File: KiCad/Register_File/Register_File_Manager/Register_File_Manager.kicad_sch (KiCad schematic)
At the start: 39 parts, among them J1 Conn_01x04_Socket, J10 Conn_01x02_Socket, J11 Conn_01x02_Socket, J12 Conn_01x02_Socket, J13 Conn_01x02_Socket, J14 Conn_01x02_Socket, J15 Conn_01x02_Socket, J16 Conn_01x02_Socket, J17 Conn_01x02_Socket, J18 Conn_01x02_Socket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

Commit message: finished registier file boards
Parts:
- removed D0, D5, D6, D7: LED, LED_THT:LED_Rectangular_W3.0mm_H2.0mm, symbol Device:LED
- removed RN1: R_Network08_US, Resistor_THT:R_Array_SIP9, symbol Device:R_Network08_US
- added J21, J22, J23, J24: Conn_01x08_Socket, Connector_PinHeader_2.54mm:PinHeader_1x08_P2.54mm_Vertical, symbol Connector:Conn_01x08_Socket
- added R1, R2, R3, R4: 1k, Resistor_SMD:R_1206_3216Metric_Pad1.30x1.75mm_HandSolder, symbol Device:R_US
- added SW1: SW_SPDT, Button_Switch_THT:SW_Slide_SPDT_Angled_CK_OS102011MA1Q, symbol Switch:SW_SPDT
- added U7: 74LS245, Package_DIP:DIP-20_W7.62mm_Socket_LongPads, symbol 74xx:74LS245
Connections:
- net GND: now also D1.1 (K), D2.1 (K), D3.1 (K), D4.1 (K), SW1.1 (A), U7.10 (GND)
- net IN_EN_REG_0: now also J23.8 (Pin_8)
- net IN_EN_REG_1: now also J23.7 (Pin_7)
- net IN_EN_REG_10: now also J24.6 (Pin_6)
- net IN_EN_REG_11: now also J24.5 (Pin_5)
- net IN_EN_REG_12: now also J24.4 (Pin_4)
- net IN_EN_REG_13: now also J24.3 (Pin_3)
- net IN_EN_REG_14: now also J24.2 (Pin_2)
- net IN_EN_REG_15: now also J24.1 (Pin_1)
- net IN_EN_REG_2: now also J23.6 (Pin_6)
- net IN_EN_REG_3: now also J23.5 (Pin_5)
- net IN_EN_REG_4: now also J23.4 (Pin_4)
- net IN_EN_REG_5: now also J23.3 (Pin_3)
- net IN_EN_REG_6: now also J23.2 (Pin_2)
- net IN_EN_REG_7: now also J23.1 (Pin_1)
- net IN_EN_REG_8: now also J24.8 (Pin_8)
- net IN_EN_REG_9: now also J24.7 (Pin_7)
- net OUT_EN_REG_0: now also J21.8 (Pin_8)
- net OUT_EN_REG_1: now also J21.7 (Pin_7)
- net OUT_EN_REG_10: now also J22.6 (Pin_6)
- net OUT_EN_REG_11: now also J22.5 (Pin_5)
- net OUT_EN_REG_12: now also J22.4 (Pin_4)
- net OUT_EN_REG_13: now also J22.3 (Pin_3)
- net OUT_EN_REG_14: now also J22.2 (Pin_2)
- net OUT_EN_REG_15: now also J22.1 (Pin_1)
- net OUT_EN_REG_2: now also J21.6 (Pin_6)
- net OUT_EN_REG_3: now also J21.5 (Pin_5)
- net OUT_EN_REG_4: now also J21.4 (Pin_4)
- net OUT_EN_REG_5: now also J21.3 (Pin_3)
- net OUT_EN_REG_6: now also J21.2 (Pin_2)
- net OUT_EN_REG_7: now also J21.1 (Pin_1)
- net OUT_EN_REG_8: now also J22.8 (Pin_8)
- net OUT_EN_REG_9: now also J22.7 (Pin_7)
- net SELECTED_REG_0: now also U7.2 (A0)
- net SELECTED_REG_1: now also U7.3 (A1)
- net SELECTED_REG_2: now also U7.4 (A2)
- net SELECTED_REG_3: now also U2.4 (E1), U2.5 (E2), U4.4 (E1), U4.5 (E2), U6.9, U7.5 (A3); no longer U3.4 (E1), U3.5 (E2), U5.4 (E1), U5.5 (E2), U6.3
- net SELECTED_REG_3_B: now also U3.4 (E1), U3.5 (E2), U5.4 (E1), U5.5 (E2), U6.8; no longer U2.4 (E1), U2.5 (E2), U4.4 (E1), U4.5 (E2), U6.4
- net VCC: now also SW1.3 (C), U7.1 (A->B), U7.20 (VCC)
- net at D2.2 (A): now also R2.2
- net at D4.2 (A): now also R4.2
- net at D1.2 (A): now also R1.2
- net at D3.2 (A): now also R3.2
- new net: SW1.2 (B), U7.19 (CE)
- new net LED_0: R1.1, U7.18 (B0)
- new net LED_1: R2.1, U7.17 (B1)
- new net LED_2: R3.1, U7.16 (B2)
- new net LED_3: R4.1, U7.15 (B3)
- no-connect marks 0 -> 8
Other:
- note added: "Data LED's"
- note added: "Test Headers"
- note removed: "LED incdicators"
- moved on the sheet: J1, J10, J11, J12, J13, J14, J15, J16, J17, J18, J19, J2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

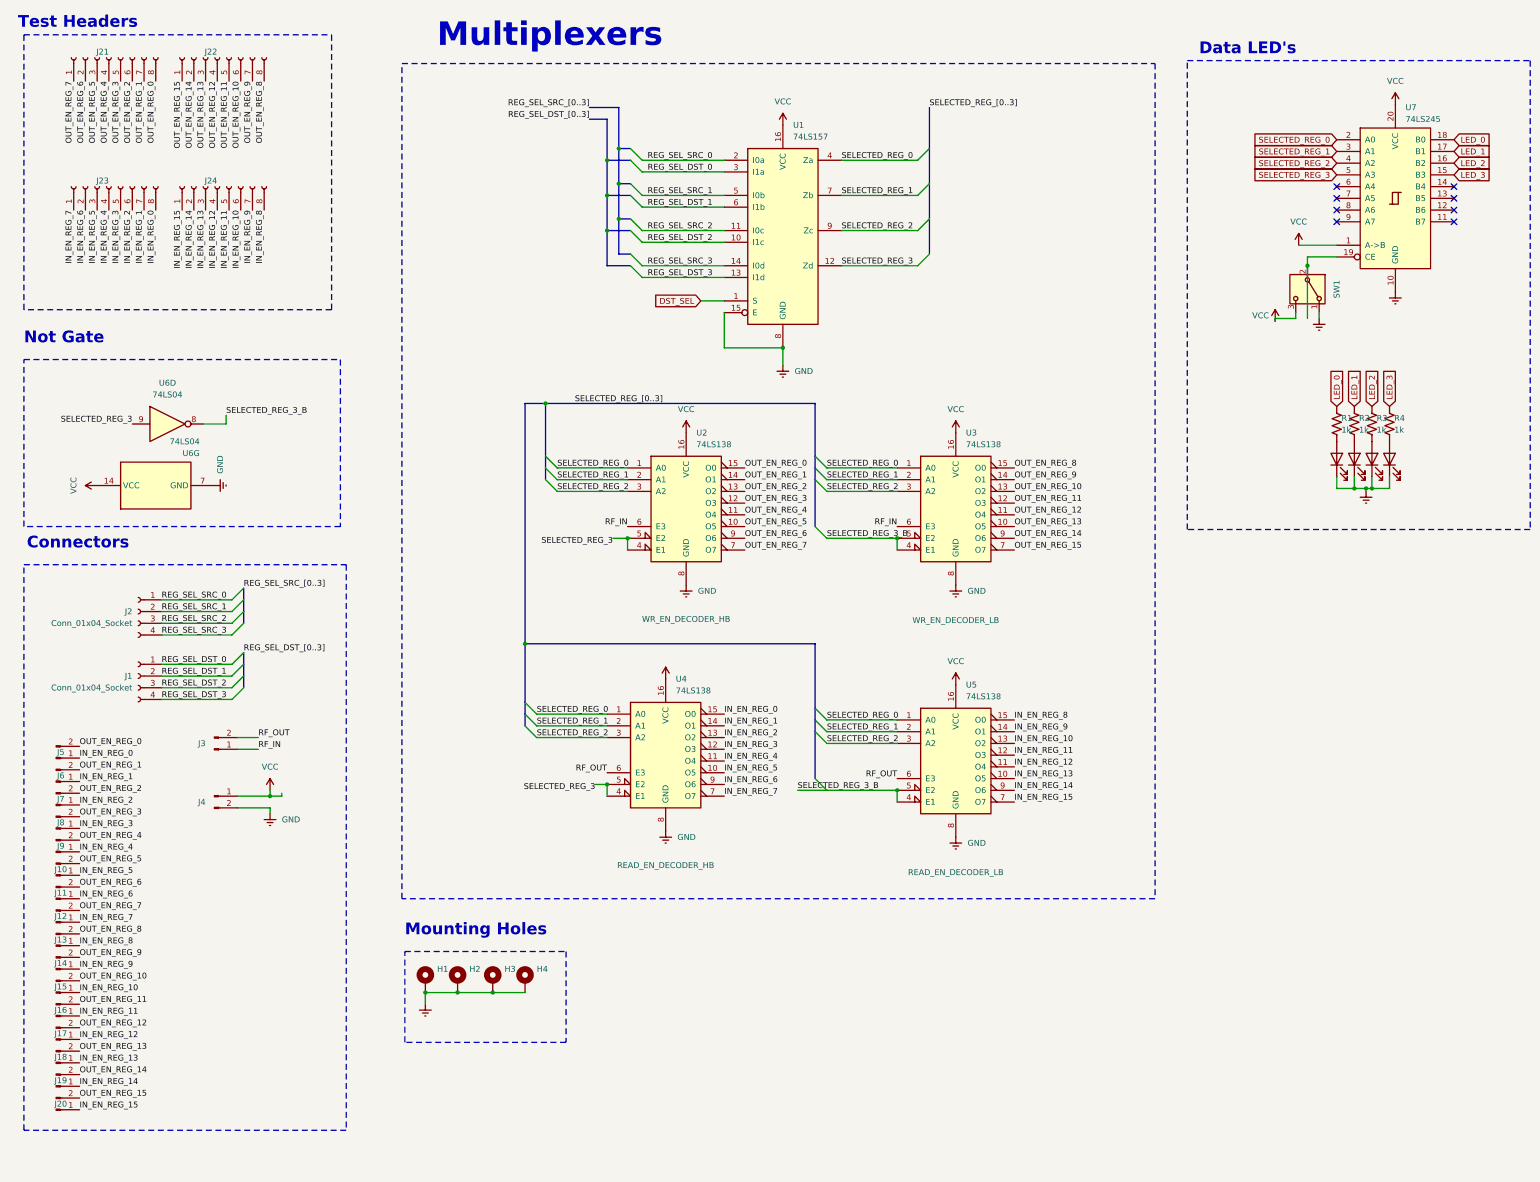
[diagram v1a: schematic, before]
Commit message: created standarts for PCB's
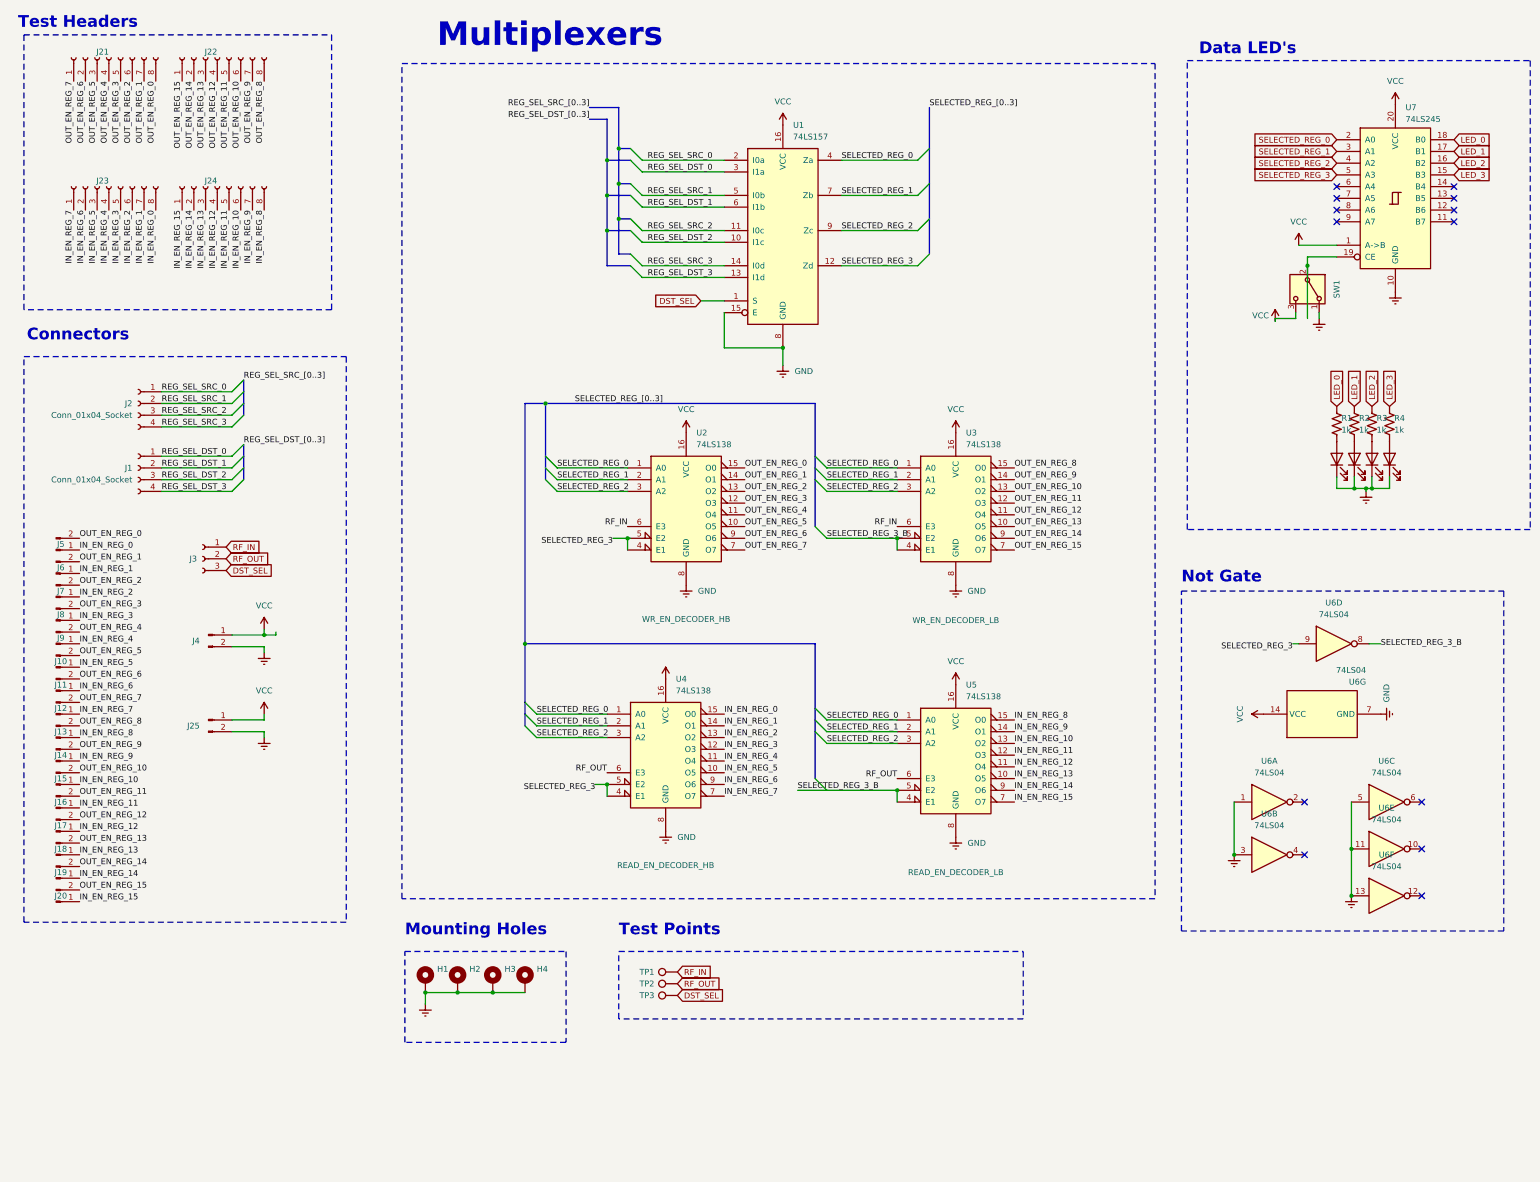
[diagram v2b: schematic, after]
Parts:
- removed J3: Conn_01x02_Socket, Connector_JST:JST_XH_S2B-XH-A-1_1x02_P2.50mm_Horizontal, symbol Connector:Conn_01x02_Pin
- added J25: Conn_01x02_Socket, Connector_JST:JST_XH_S2B-XH-A-1_1x02_P2.50mm_Horizontal, symbol Connector:Conn_01x02_Pin
- added J3: Conn_01x03_Socket, Connector_JST:JST_XH_S3B-XH-A-1_1x03_P2.50mm_Horizontal, symbol Connector:Conn_01x03_Socket
- added TP1, TP2, TP3: TestPoint, TestPoint:TestPoint_Pad_D1.0mm, symbol Connector:TestPoint
- added unit 2 of U6
- added unit 1 of U6
- added unit 3 of U6
- added unit 5 of U6
- added unit 6 of U6
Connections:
- net DST_SEL: now also J3.3 (Pin_3), TP3.1
- net GND: now also J25.2 (Pin_2), U6.1, U6.11, U6.13, U6.3, U6.5
- net RF_IN: now also J3.1 (Pin_1), TP1.1
- net RF_OUT: now also J3.2 (Pin_2), TP2.1
- net VCC: now also J25.1 (Pin_1)
- no-connect marks 8 -> 13
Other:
- note added: "Test Points"
- moved on the sheet: J1, J10, J11, J12, J13, J14, J15, J16, J17, J18, J19, J2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
